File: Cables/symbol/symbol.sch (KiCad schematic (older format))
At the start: 22 parts, among them J1 Atari5200_Famicom_NeoGeoAES_P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, J10 Dreamcast, J11 PSX_PS2, J2 Atari_SEGA_DE9, J3 NES, J4 N64, J6 SFC_SNES, J7 GameCube, J9 Saturn

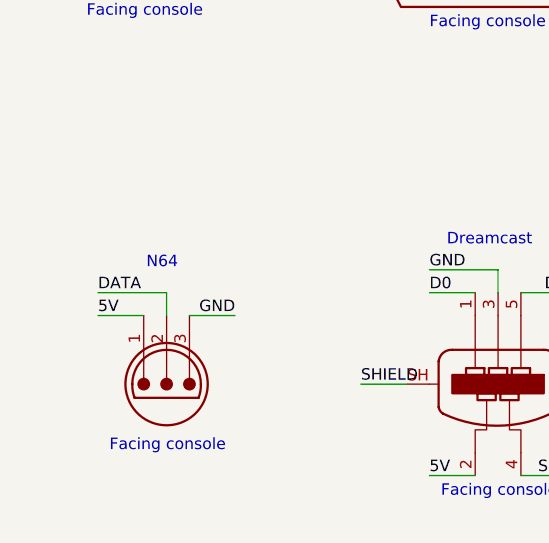
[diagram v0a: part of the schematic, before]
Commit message: Update adapter cable schematics
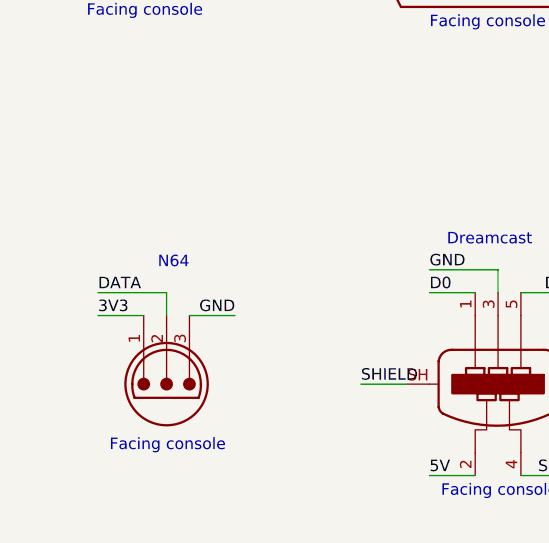
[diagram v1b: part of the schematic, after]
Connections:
- net 3V3: now also J4.1
- net 5V: no longer J4.1
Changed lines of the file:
@@
 Sheet 1 1
 Title "BlueRetro - Controller pinout reference"
-Date "2020-10-02"
-Rev "v1.0"
+Date "2020-11-03"
+Rev "v1.0.1"
 Comp "©2020 Jacques Gagnon, licensed under CC-BY-4.0"
 Comment1 ""
@@
 Text Notes 8200 4900 2    50   ~ 0
 PSX / PS2
-Text Notes 1300 6750 2    50   ~ 0
+Text Notes 1350 6750 2    50   ~ 0
 N64
 Text Notes 6250 4800 2    50   ~ 0
@@
 DATA
 Text Label 950  6950 0    50   ~ 0
-5V
+3V3
 Wire Wire Line
 	1250 6850 950  6850

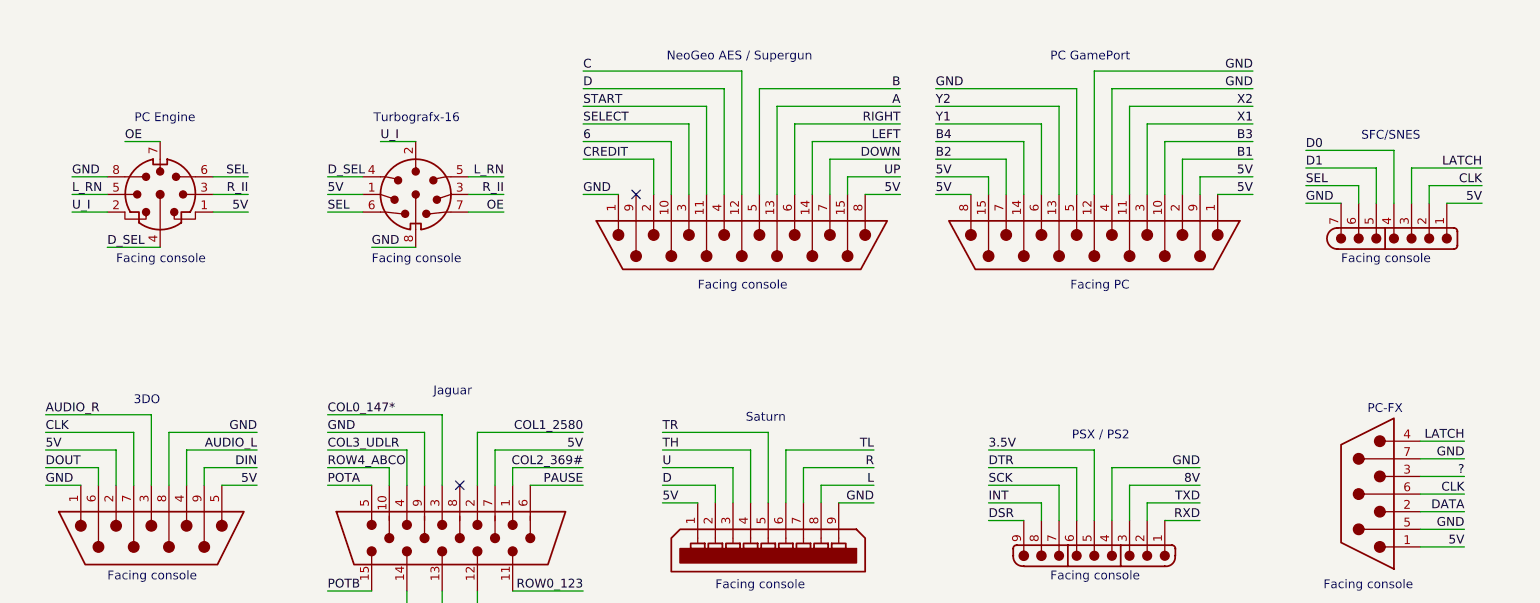
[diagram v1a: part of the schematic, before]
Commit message: Update NEC pinouts
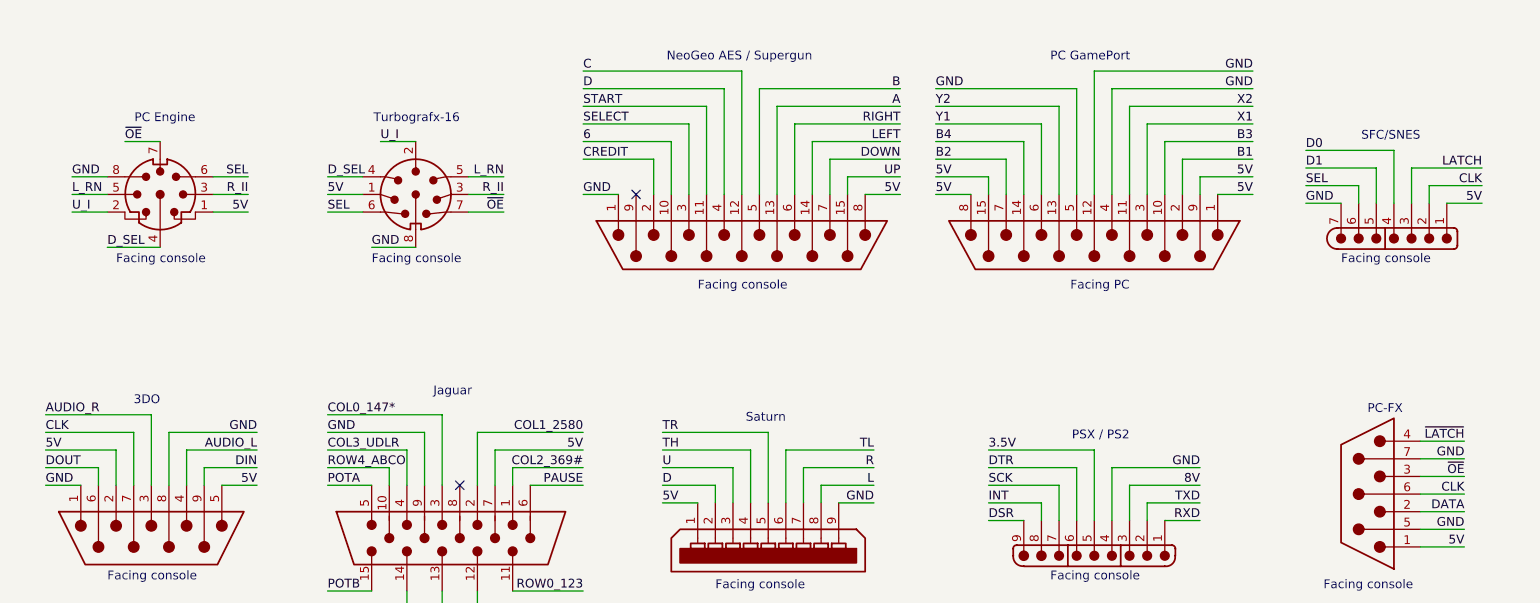
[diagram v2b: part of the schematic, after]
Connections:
- net OE is gone; now on net ~OE~: J?.7, J?.7
- net LATCH: no longer J?.4
- net ? renamed ~OE~
- new net ~LATCH~: J?.4
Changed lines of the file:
@@
 Sheet 1 1
 Title "BlueRetro - Controller pinout reference"
-Date "2020-11-03"
-Rev "v1.0.1"
-Comp "©2020 Jacques Gagnon, licensed under CC-BY-4.0"
+Date "2021-04-01"
+Rev "v1.1"
+Comp "©2020-2021 Jacques Gagnon, licensed under CC-BY-4.0"
 Comment1 ""
 Comment2 ""
@@
 SEL
 Text Label 2500 3200 0    50   ~ 0
-OE
+~OE~
 Text Label 2200 3400 0    50   ~ 0
 GND
@@
 R_II
 Text Label 4650 3600 2    50   ~ 0
-OE
+~OE~
 Text Label 3900 3800 0    50   ~ 0
 GND
@@
 DATA
 Text Label 10100 5100 2    50   ~ 0
-?
+~OE~
 Text Label 10100 4900 2    50   ~ 0
-LATCH
+~LATCH~
 Wire Wire Line
 	9850 5500 10100 5500

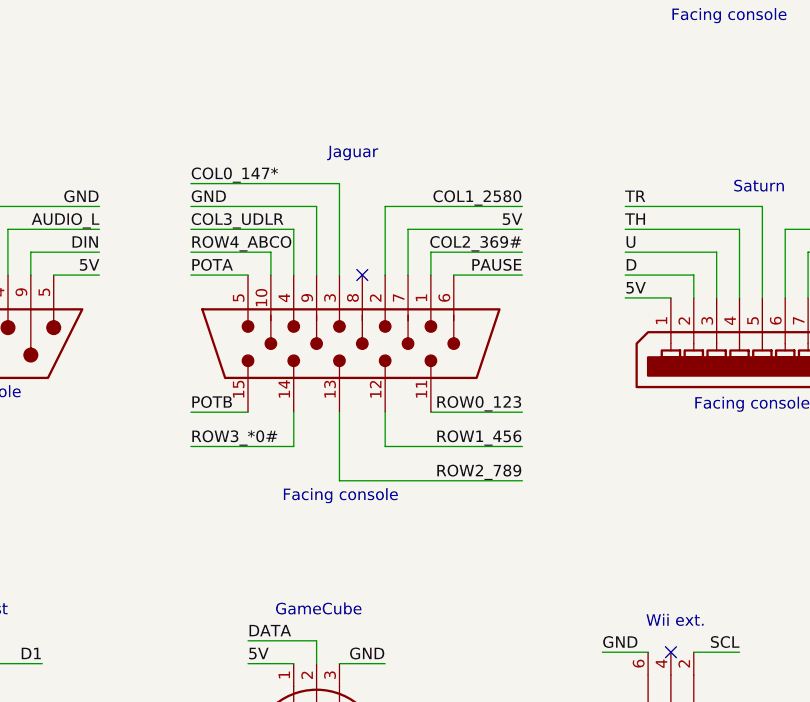
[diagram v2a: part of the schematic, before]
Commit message: [DIY] Add Jaguar adapter cable
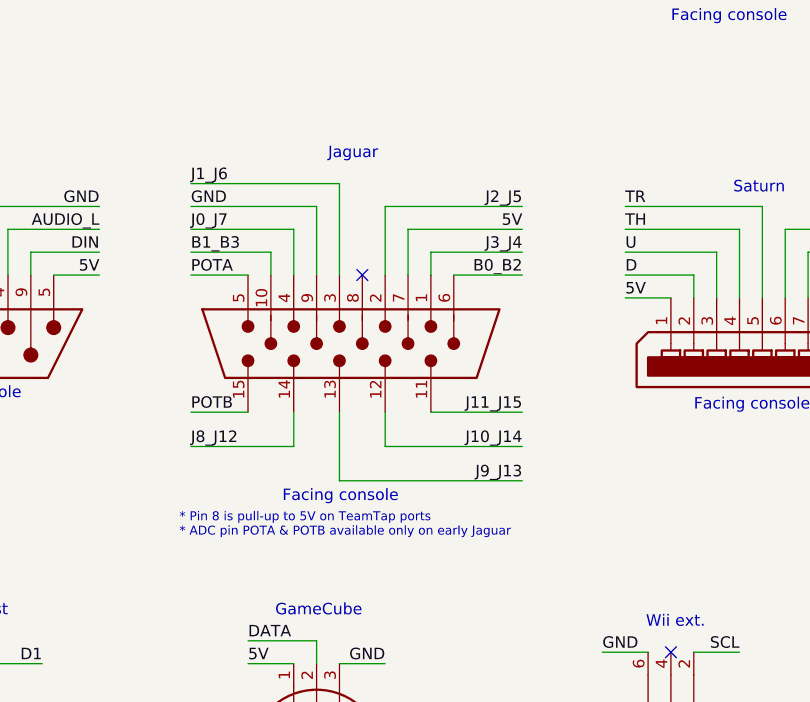
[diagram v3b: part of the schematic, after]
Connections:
- net COL0_147*: no longer J?.3
- net COL1_2580: no longer J?.2
- net COL2_369#: no longer J?.1
- net ROW0_123: no longer J?.11
- net ROW1_456: no longer J?.12
- net ROW2_789: no longer J?.13
- net ROW3_*0#: no longer J?.14
- net COL3_UDLR renamed J0_J7
- net PAUSE renamed B0_B2
- net ROW4_ABCO renamed B1_B3
- new net J10_J14: J?.12
- new net J11_J15: J?.11
- new net J1_J6: J?.3
- new net J2_J5: J?.2
- new net J3_J4: J?.1
- new net J8_J12: J?.14
- new net J9_J13: J?.13
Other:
- note added: "* Pin 8 is pull-up to 5V on TeamTap ports\n* ADC pin POTA & POTB available only on early Jaguar"
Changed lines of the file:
@@
 5V
 Text Label 3650 4750 0    50   ~ 0
-COL0_147*
+J1_J6
 Text Label 5100 4850 2    50   ~ 0
-COL1_2580
+J2_J5
 Text Label 5100 5050 2    50   ~ 0
-COL2_369#
+J3_J4
 Text Label 3650 4950 0    50   ~ 0
-COL3_UDLR
+J0_J7
 Text Label 5100 5750 2    50   ~ 0
-ROW0_123
+J11_J15
 Wire Wire Line
 	4700 5750 5100 5750
 Text Label 5100 5900 2    50   ~ 0
-ROW1_456
+J10_J14
 Text Label 5100 6050 2    50   ~ 0
-ROW2_789
+J9_J13
 Text Label 3650 5900 0    50   ~ 0
-ROW3_*0#
+J8_J12
 Wire Wire Line
 	4500 5900 5100 5900
@@
 	4300 6050 5100 6050
 Text Label 3650 5050 0    50   ~ 0
-ROW4_ABCO
+B1_B3
 Wire Wire Line
 	3650 5050 4000 5050
@@
 	4500 4850 5100 4850
 Text Label 5100 5150 2    50   ~ 0
-PAUSE
+B0_B2
 Text Label 3650 5150 0    50   ~ 0
 POTA
@@
 Text Notes 5750 4050 0    50   ~ 0
 Facing console
+Text Notes 3600 6300 0    39   ~ 0
+* Pin 8 is pull-up to 5V on TeamTap ports\n* ADC pin POTA & POTB available only on early Jaguar
 $EndSCHEMATC

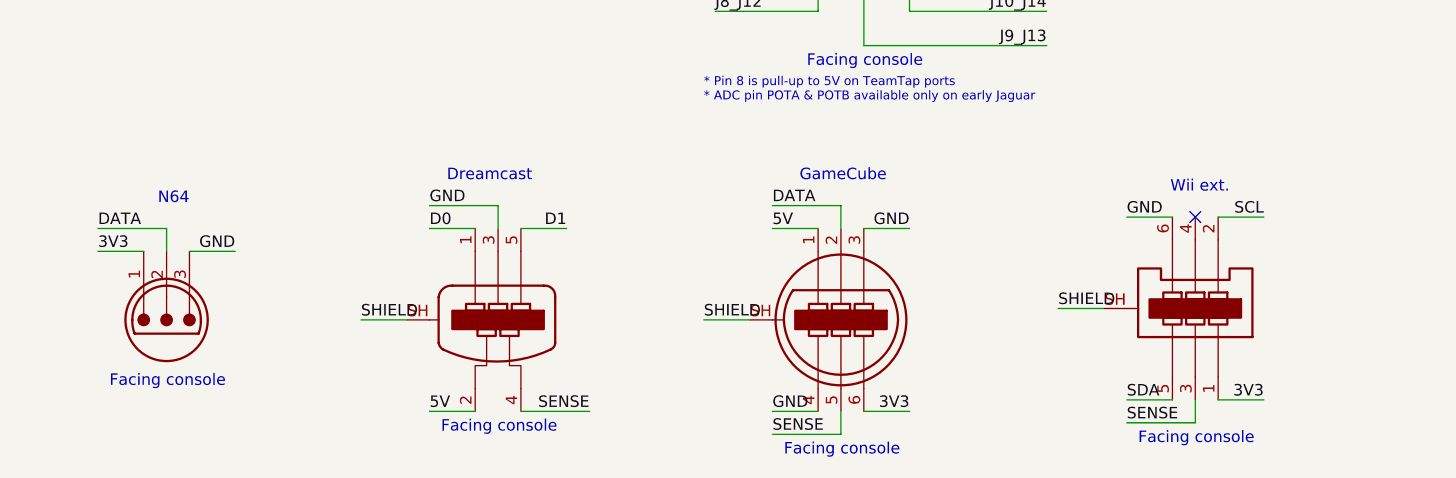
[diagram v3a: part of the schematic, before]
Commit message: [Cables] Add Virtual Boy connector symbol
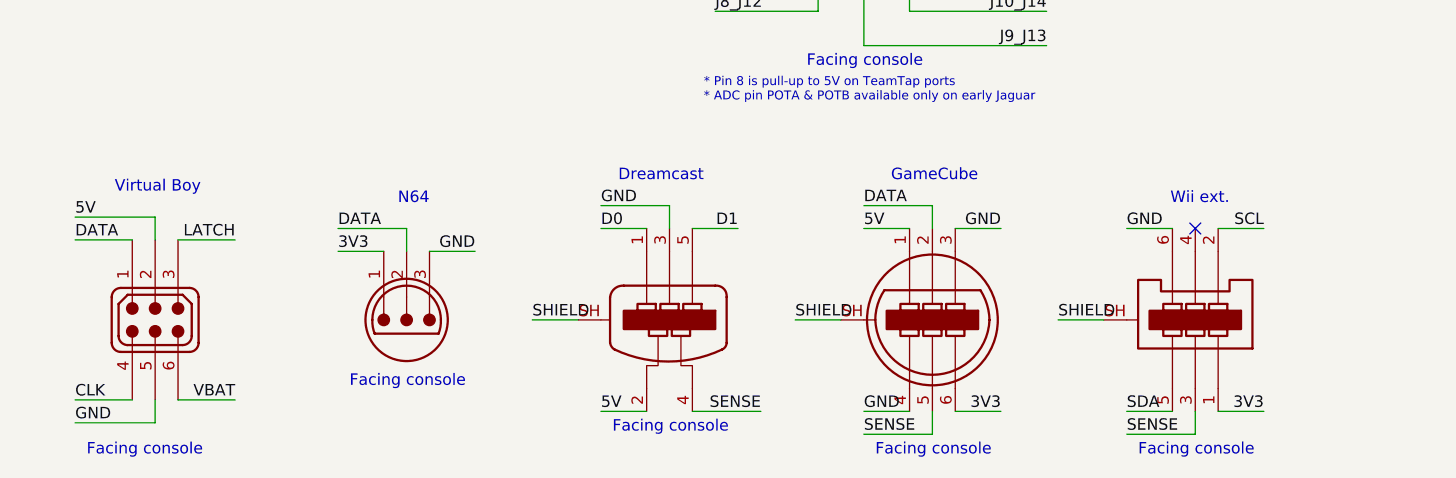
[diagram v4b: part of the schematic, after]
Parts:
- added J?: VB, symbol Connector_Gaming:VB
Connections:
- net 5V: now also J?.2
- net CLK: now also J?.4
- net DATA: now also J?.1
- net GND: now also J?.5
- net LATCH: now also J?.3
- new net VBAT: J?.6
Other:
- note added: "Virtual Boy"
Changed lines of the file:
@@
 Sheet 1 1
 Title "BlueRetro - Controller pinout reference"
-Date "2021-04-01"
-Rev "v1.1"
-Comp "©2020-2021 Jacques Gagnon, licensed under CC-BY-4.0"
+Date "2022-01-10"
+Rev "v1.2"
+Comp "©2020-2022 Jacques Gagnon, licensed under CC-BY-4.0"
 Comment1 ""
 Comment2 ""
@@
 L Connector_Gaming:GameCube J7
 U 1 1 5F78A04A
-P 4700 7150
-F 0 "J7" H 4800 7101 50  0001 C CNN
-F 1 "GameCube" H 4800 7010 50  0001 C CNN
-F 2 "" H 4700 7150 50  0001 C CNN
-F 3 "" H 4700 7150 50  0001 C CNN
-	1    4700 7150
+P 5100 7150
+F 0 "J7" H 5200 7101 50  0001 C CNN
+F 1 "GameCube" H 5200 7010 50  0001 C CNN
+F 2 "" H 5100 7150 50  0001 C CNN
+F 3 "" H 5100 7150 50  0001 C CNN
+	1    5100 7150
 	0    1    1    0
 $EndComp
@@
 L Connector_Gaming:Dreamcast J10
 U 1 1 5F78F2E6
-P 3200 7150
-F 0 "J10" H 3300 7065 50  0001 C CNN
-F 1 "Dreamcast" H 3300 6974 50  0001 C CNN
-F 2 "" H 3200 7150 50  0001 C CNN
-F 3 "" H 3200 7150 50  0001 C CNN
-	1    3200 7150
+P 3950 7150
+F 0 "J10" H 4050 7065 50  0001 C CNN
+F 1 "Dreamcast" H 4050 6974 50  0001 C CNN
+F 2 "" H 3950 7150 50  0001 C CNN
+F 3 "" H 3950 7150 50  0001 C CNN
+	1    3950 7150
 	0    1    1    0
 $EndComp
@@
 LATCH
 Wire Wire Line
-	4100 6850 3900 6850
-Wire Wire Line
-	3800 7250 3600 7250
-Wire Wire Line
-	4300 6850 4500 6850
-Wire Wire Line
-	4300 7650 4500 7650
-Wire Wire Line
-	4100 7650 3900 7650
-Wire Wire Line
-	4200 6850 4200 6750
-Wire Wire Line
-	4200 6750 3900 6750
-Wire Wire Line
-	4200 7650 4200 7750
-Wire Wire Line
-	4200 7750 3900 7750
-Text Label 3600 7250 0    50   ~ 0
+	4500 6850 4300 6850
+Wire Wire Line
+	4200 7250 4000 7250
+Wire Wire Line
+	4700 6850 4900 6850
+Wire Wire Line
+	4700 7650 4900 7650
+Wire Wire Line
+	4500 7650 4300 7650
+Wire Wire Line
+	4600 6850 4600 6750
+Wire Wire Line
+	4600 6750 4300 6750
+Wire Wire Line
+	4600 7650 4600 7750
+Wire Wire Line
+	4600 7750 4300 7750
+Text Label 4000 7250 0    50   ~ 0
 SHIELD
-Text Label 3900 6850 0    50   ~ 0
-5V
-Text Label 3900 6750 0    50   ~ 0
+Text Label 4300 6850 0    50   ~ 0
+5V
+Text Label 4300 6750 0    50   ~ 0
 DATA
-Text Label 3900 7650 0    50   ~ 0
-GND
-Text Label 3900 7750 0    50   ~ 0
+Text Label 4300 7650 0    50   ~ 0
+GND
+Text Label 4300 7750 0    50   ~ 0
 SENSE
-Text Label 4500 6850 2    50   ~ 0
-GND
-Text Label 4500 7650 2    50   ~ 0
+Text Label 4900 6850 2    50   ~ 0
+GND
+Text Label 4900 7650 2    50   ~ 0
 3V3
 Wire Wire Line
-	2600 6850 2400 6850
-Wire Wire Line
-	2800 6850 3000 6850
-Wire Wire Line
-	2600 7650 2400 7650
-Wire Wire Line
-	2700 6850 2700 6750
-Wire Wire Line
-	2700 6750 2400 6750
-Text Label 2400 6850 0    50   ~ 0
+	3350 6850 3150 6850
+Wire Wire Line
+	3550 6850 3750 6850
+Wire Wire Line
+	3350 7650 3150 7650
+Wire Wire Line
+	3450 6850 3450 6750
+Wire Wire Line
+	3450 6750 3150 6750
+Text Label 3150 6850 0    50   ~ 0
 D0
-Text Label 2400 7650 0    50   ~ 0
-5V
-Text Label 2400 6750 0    50   ~ 0
-GND
-Text Label 3000 6850 2    50   ~ 0
+Text Label 3150 7650 0    50   ~ 0
+5V
+Text Label 3150 6750 0    50   ~ 0
+GND
+Text Label 3750 6850 2    50   ~ 0
 D1
-Text Label 3100 7650 2    50   ~ 0
+Text Label 3850 7650 2    50   ~ 0
 SENSE
 Wire Wire Line
-	2800 7650 3100 7650
+	3550 7650 3850 7650
 Wire Wire Line
 	8850 1450 8650 1450
@@
 C
 NoConn ~ 5400 3500
-Text Notes 3950 7850 0    50   ~ 0
-Facing console
-Text Notes 2450 7750 0    50   ~ 0
+Text Notes 4350 7850 0    50   ~ 0
+Facing console
+Text Notes 3200 7750 0    50   ~ 0
 Facing console
 Text Notes 9400 3900 0    50   ~ 0
@@
 L Connector_Gaming:Wii J?
 U 1 1 5FA65026
-P 6250 7100
-F 0 "J?" V 6304 6880 50  0001 L CNN
-F 1 "Wii" V 6395 6880 50  0001 L CNN
-F 2 "" H 6250 7100 50  0001 C CNN
-F 3 "" H 6250 7100 50  0001 C CNN
-	1    6250 7100
-	0    1    1    0
-$EndComp
-Wire Wire Line
-	5650 6800 5450 6800
-Wire Wire Line
-	5350 7200 5150 7200
-Wire Wire Line
-	5850 6800 6050 6800
-Wire Wire Line
-	5850 7600 6050 7600
-Wire Wire Line
-	5650 7600 5450 7600
-Wire Wire Line
-	5750 7600 5750 7700
-Wire Wire Line
-	5750 7700 5450 7700
-Text Label 5150 7200 0    50   ~ 0
+P 6250 7150
+F 0 "J?" V 6304 6930 50  0001 L CNN
+F 1 "Wii" V 6395 6930 50  0001 L CNN
+F 2 "" H 6250 7150 50  0001 C CNN
+F 3 "" H 6250 7150 50  0001 C CNN
+	1    6250 7150
+	0    1    1    0
+$EndComp
+Wire Wire Line
+	5650 6850 5450 6850
+Wire Wire Line
+	5350 7250 5150 7250
+Wire Wire Line
+	5850 6850 6050 6850
+Wire Wire Line
+	5850 7650 6050 7650
+Wire Wire Line
+	5650 7650 5450 7650
+Wire Wire Line
+	5750 7650 5750 7750
+Wire Wire Line
+	5750 7750 5450 7750
+Text Label 5150 7250 0    50   ~ 0
 SHIELD
-Text Label 5450 6800 0    50   ~ 0
-GND
-Text Label 5450 7600 0    50   ~ 0
+Text Label 5450 6850 0    50   ~ 0
+GND
+Text Label 5450 7650 0    50   ~ 0
 SDA
-Text Label 5450 7700 0    50   ~ 0
+Text Label 5450 7750 0    50   ~ 0
 SENSE
-Text Label 6050 6800 2    50   ~ 0
+Text Label 6050 6850 2    50   ~ 0
 SCL
-Text Label 6050 7600 2    50   ~ 0
+Text Label 6050 7650 2    50   ~ 0
 3V3
-Text Notes 5500 7800 0    50   ~ 0
-Facing console
-NoConn ~ 5750 6800
+Text Notes 5500 7850 0    50   ~ 0
+Facing console
+NoConn ~ 5750 6850
 Text Notes 1300 3200 2    50   ~ 0
 NES
 Text Notes 9850 3200 2    50   ~ 0
 SFC/SNES
-Text Notes 4400 6650 2    50   ~ 0
+Text Notes 4800 6650 2    50   ~ 0
 GameCube
-Text Notes 2850 6650 2    50   ~ 0
+Text Notes 3600 6650 2    50   ~ 0
 Dreamcast
 Text Notes 2700 4700 2    50   ~ 0
@@
 Text Notes 4400 3100 2    50   ~ 0
 Turbografx-16
-Text Notes 5900 6700 2    50   ~ 0
+Text Notes 5900 6750 2    50   ~ 0
 Wii ext.
 Wire Wire Line
@@
 Text Notes 8200 4900 2    50   ~ 0
 PSX / PS2
-Text Notes 1350 6750 2    50   ~ 0
+Text Notes 2400 6750 2    50   ~ 0
 N64
 Text Notes 6250 4800 2    50   ~ 0
@@
 Text Notes 5850 5750 0    50   ~ 0
 Facing console
-Text Notes 1000 7550 0    50   ~ 0
-Facing console
-Text Label 2100 7250 0    50   ~ 0
+Text Notes 2050 7550 0    50   ~ 0
+Facing console
+Text Label 2850 7250 0    50   ~ 0
 SHIELD
 Wire Wire Line
-	2300 7250 2100 7250
-Text Label 1550 6950 2    50   ~ 0
-GND
-Text Label 950  6850 0    50   ~ 0
+	3050 7250 2850 7250
+Text Label 2600 6950 2    50   ~ 0
+GND
+Text Label 2000 6850 0    50   ~ 0
 DATA
-Text Label 950  6950 0    50   ~ 0
+Text Label 2000 6950 0    50   ~ 0
 3V3
 Wire Wire Line
-	1250 6850 950  6850
-Wire Wire Line
-	1250 6950 1250 6850
-Wire Wire Line
-	1350 6950 1550 6950
-Wire Wire Line
-	1150 6950 950  6950
+	2300 6850 2000 6850
+Wire Wire Line
+	2300 6950 2300 6850
+Wire Wire Line
+	2400 6950 2600 6950
+Wire Wire Line
+	2200 6950 2000 6950
 Text Label 6750 5250 2    50   ~ 0
 GND
@@
 L Connector_Gaming:N64 J4
 U 1 1 5F784AB6
-P 1150 7250
-F 0 "J4" H 1358 7396 50  0001 L CNN
-F 1 "N64" H 1358 7305 50  0001 L CNN
-F 2 "" H 1190 7310 50  0001 C CNN
-F 3 "" H 1190 7310 50  0001 C CNN
-	1    1150 7250
+P 2200 7250
+F 0 "J4" H 2408 7396 50  0001 L CNN
+F 1 "N64" H 2408 7305 50  0001 L CNN
+F 2 "" H 2240 7310 50  0001 C CNN
+F 3 "" H 2240 7310 50  0001 C CNN
+	1    2200 7250
 	0    1    1    0
 $EndComp
@@
 Text Notes 3600 6300 0    39   ~ 0
 * Pin 8 is pull-up to 5V on TeamTap ports\n* ADC pin POTA & POTB available only on early Jaguar
+$Comp
+L Connector_Gaming:VB J?
+U 1 1 61E14252
+P 1200 7200
+F 0 "J?" H 1250 7557 50  0001 C CNN
+F 1 "VB" H 1250 7466 50  0001 C CNN
+F 2 "" H 1240 7260 50  0001 C CNN
+F 3 "" H 1240 7260 50  0001 C CNN
+	1    1200 7200
+	0    1    1    0
+$EndComp
+Wire Wire Line
+	1300 6900 1550 6900
+Wire Wire Line
+	1300 7600 1550 7600
+Wire Wire Line
+	850  6900 1100 6900
+Wire Wire Line
+	850  7600 1100 7600
+Wire Wire Line
+	1200 6900 1200 6800
+Wire Wire Line
+	1200 6800 850  6800
+Wire Wire Line
+	1200 7600 1200 7700
+Wire Wire Line
+	1200 7700 850  7700
+Text Notes 1400 6700 2    50   ~ 0
+Virtual Boy
+Text Notes 900  7850 0    50   ~ 0
+Facing console
+Text Label 850  6900 0    50   ~ 0
+DATA
+Text Label 1550 6900 2    50   ~ 0
+LATCH
+Text Label 850  7600 0    50   ~ 0
+CLK
+Text Label 850  7700 0    50   ~ 0
+GND
+Text Label 1550 7600 2    50   ~ 0
+VBAT
+Text Label 850  6800 0    50   ~ 0
+5V
 $EndSCHEMATC
